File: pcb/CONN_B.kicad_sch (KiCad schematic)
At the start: 8 parts, among them J2 USB_B, J3 6437288-4, J4 Conn_ARM_SWD_TagConnect_TC2030

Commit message: power done
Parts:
- removed R1, R2, R3, R4: 47R, Resistor_SMD:R_0603_1608Metric_Pad0.98x0.95mm_HandSolder, symbol Device:R
- added JP2: SolderJumper_2_Open, symbol Jumper:SolderJumper_2_Open
- J4: value Conn_ARM_SWD_TagConnect_TC2030 -> TagConnect
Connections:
- net 3V3: now also JP2.2 (B); no longer J4.1 (VCC)
- net STM_NRST: now also J3.19, J4.3 (~{RESET})
- net STM_SWDCLK: now also J3.17, J4.4 (SWCLK)
- net STM_SWDIO: now also J3.16, J4.2 (SWDIO)
- net STM_SWO: now also J3.18, J4.6 (SWO)
- net GPIO_3V3: now reaches J3.11
- new net: J4.1 (VCC), JP2.1 (A)
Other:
- moved on the sheet: C1, J2, J3, J4

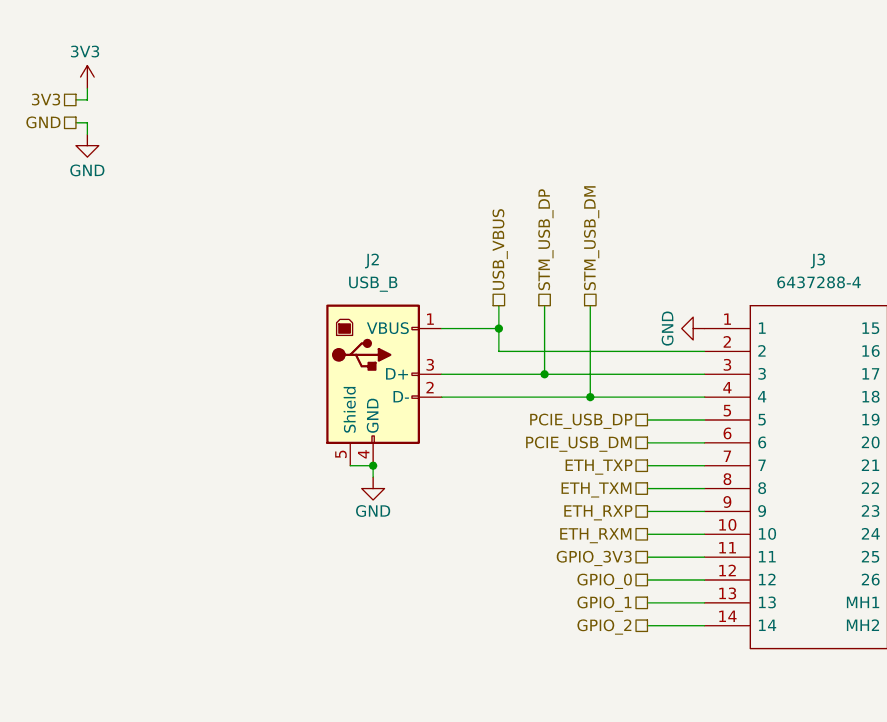
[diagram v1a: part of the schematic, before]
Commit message: added USB protection, reviewed LSD and HSD, improved input TVS footprint
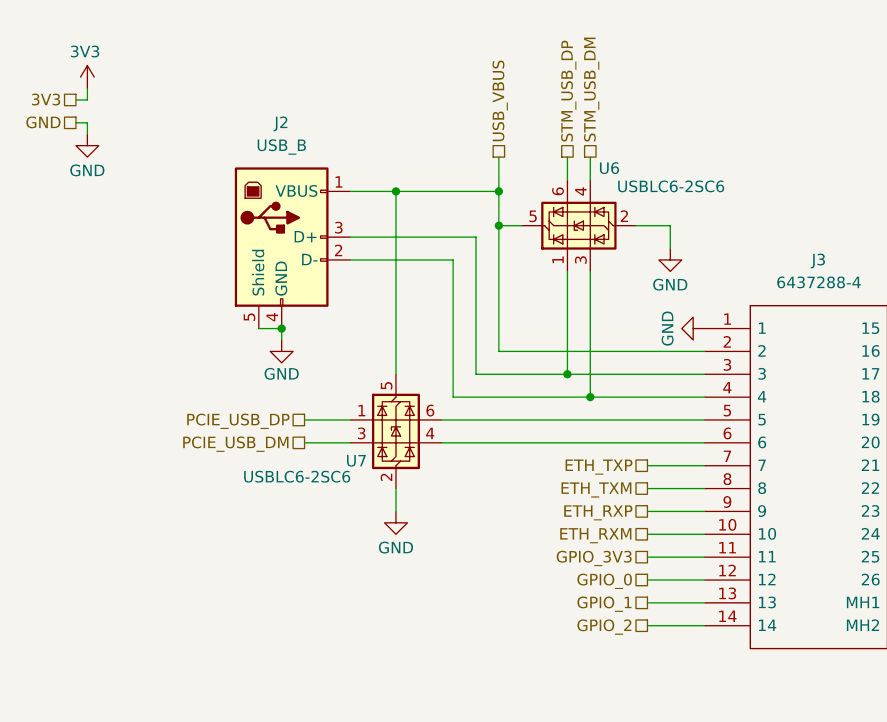
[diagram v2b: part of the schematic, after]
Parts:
- added U6, U7: USBLC6-2SC6, Package_TO_SOT_SMD:SOT-23-6, symbol Power_Protection:USBLC6-2SC6
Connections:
- net GND: now also U6.2 (GND), U7.2 (GND)
- net PCIE_USB_DM: now also U7.3 (I/O2); no longer J3.6
- net PCIE_USB_DP: now also U7.1 (I/O1); no longer J3.5
- net STM_USB_DM: now also U6.4 (I/O2); no longer J2.2 (D-), J3.4
- net STM_USB_DP: now also U6.6 (I/O1); no longer J2.3 (D+), J3.3
- net USB_VBUS: now also U6.5 (VBUS), U7.5 (VBUS)
- new net: J2.2 (D-), J3.4, U6.3 (I/O2)
- new net: J2.3 (D+), J3.3, U6.1 (I/O1)
- new net: J3.5, U7.6 (I/O1)
- new net: J3.6, U7.4 (I/O2)
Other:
- moved on the sheet: J2

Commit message: reannotated, updated some symbols
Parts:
- removed JP2: SolderJumper_2_Open, symbol Jumper:SolderJumper_2_Open
- added JP1, JP2, JP3, JP4, JP5: SolderJumper_2_Bridged, Jumper:SolderJumper-2_P1.3mm_Bridged_RoundedPad1.0x1.5mm, symbol Jumper:SolderJumper_2_Bridged
- renumbered U7 to U1, U6 to U2
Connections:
- net 3V3: now also JP5.2 (B)
- net STM_NRST: now also JP4.2 (B); no longer J3.19
- net STM_SWDCLK: now also JP2.2 (B); no longer J3.17
- net STM_SWDIO: now also JP1.2 (B); no longer J3.16
- net STM_SWO: now also JP3.2 (B); no longer J3.18
- net at J4.1 (VCC): now also JP5.1 (A)
- new net: J3.17, JP2.1 (A)
- new net: J3.16, JP1.1 (A)
- new net: J3.18, JP3.1 (A)
- new net: J3.19, JP4.1 (A)

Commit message: minor changes before layout
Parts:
- removed JP5: SolderJumper_2_Bridged, Jumper:SolderJumper-2_P1.3mm_Bridged_RoundedPad1.0x1.5mm, symbol Jumper:SolderJumper_2_Bridged
- added JP5: SolderJumper_2_Open, Jumper:SolderJumper-2_P1.3mm_Open_RoundedPad1.0x1.5mm, symbol Jumper:SolderJumper_2_Open
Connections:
- net 3V3: now also JP5.2 (B)
- net at J4.1 (VCC): now also JP5.1 (A)
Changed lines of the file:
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@@
-	)
-	(symbol
-		(lib_id "Jumper:SolderJumper_2_Bridged")
-		(at 168.91 40.64 0)
-		(unit 1)
-		(exclude_from_sim no)
-		(in_bom no)
-		(on_board yes)
-		(dnp no)
-		(property "Reference" "JP5"
-			(at 165.862 39.37 0)
-			(effects
-				(font
-					(size 1.27 1.27)
-				)
-			)
-		)
-		(property "Value" "SolderJumper_2_Bridged"
-			(at 168.91 36.83 0)
-			(effects
-				(font
-					(size 1.27 1.27)
-				)
-				(hide yes)
-			)
-		)
-		(property "Footprint" "Jumper:SolderJumper-2_P1.3mm_Bridged_RoundedPad1.0x1.5mm"
-			(at 168.91 40.64 0)
-			(effects
-				(font
-					(size 1.27 1.27)
-				)
-				(hide yes)
-			)
-		)
-		(property "Datasheet" "~"
-			(at 168.91 40.64 0)
-			(effects
-				(font
-					(size 1.27 1.27)
-				)
-				(hide yes)
-			)
-		)
-		(property "Description" "Solder Jumper, 2-pole, closed/bridged"
-			(at 168.91 40.64 0)
-			(effects
-				(font
-					(size 1.27 1.27)
-				)
-				(hide yes)
-			)
-		)
-		(pin "1"
-		)
-		(pin "2"
-		)
-		(instances
-			(project "NCU"
-				(path "/3aee14c3-5480-4f7c-989e-3fef81779034/58530478-b11f-47ae-90e9-56fd185c9f38"
-					(reference "JP5")
-					(unit 1)
-				)
-			)
-		)
 	)
 	(symbol
@@
 					(unit 1)
 				)
+			)
+		)
+	)
+	(symbol
+		(lib_id "Jumper:SolderJumper_2_Open")
+		(at 168.91 40.64 0)
+		(unit 1)
+		(exclude_from_sim no)
+		(in_bom no)
+		(on_board yes)
+		(dnp no)
+		(fields_autoplaced yes)
+		(property "Reference" "JP5"
+			(at 168.91 34.29 0)
+			(effects
+				(font
+					(size 1.27 1.27)
+				)
+			)
+		)
+		(property "Value" "SolderJumper_2_Open"
+			(at 168.91 36.83 0)
+			(effects
+				(font
+					(size 1.27 1.27)
+				)
+			)
+		)
+		(property "Footprint" "Jumper:SolderJumper-2_P1.3mm_Open_RoundedPad1.0x1.5mm"
+			(at 168.91 40.64 0)
+			(effects
+				(font
+					(size 1.27 1.27)
+				)
+				(hide yes)
+			)
+		)
+		(property "Datasheet" "~"
+			(at 168.91 40.64 0)
+			(effects
+				(font
+					(size 1.27 1.27)
+				)
+				(hide yes)
+			)
+		)
+		(property "Description" "Solder Jumper, 2-pole, open"
+			(at 168.91 40.64 0)
+			(effects
+				(font
+					(size 1.27 1.27)
+				)
+				(hide yes)
+			)
+		)
+		(pin "1"
+		)
+		(pin "2"
+		)
+		(instances
+			(project ""
+				(path "/3aee14c3-5480-4f7c-989e-3fef81779034/58530478-b11f-47ae-90e9-56fd185c9f38"
+					(reference "JP5")
+					(unit 1)
+				)

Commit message: sd card slot initial attempt (I meant SIM before)
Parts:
- J2: footprint Connector_USB:USB_B_Lumberg_2411_02_Horizontal -> Connector_USB:USB_B_OST_USB-B1HSxx_Horizontal
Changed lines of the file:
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@@
 			)
 		)
-		(property "Footprint" "Connector_USB:USB_B_Lumberg_2411_02_Horizontal"
+		(property "Footprint" "Connector_USB:USB_B_OST_USB-B1HSxx_Horizontal"
 			(at 45.72 38.1 0)
 			(effects

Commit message: rerouted usb and comms signals
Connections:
- net PCIE_USB_DM: now also U1.4 (I/O2); no longer U1.3 (I/O2)
- net PCIE_USB_DP: now also U1.6 (I/O1); no longer U1.1 (I/O1)
- net at J3.5: now also U1.1 (I/O1); no longer U1.6 (I/O1)
- net at J3.6: now also U1.3 (I/O2); no longer U1.4 (I/O2)

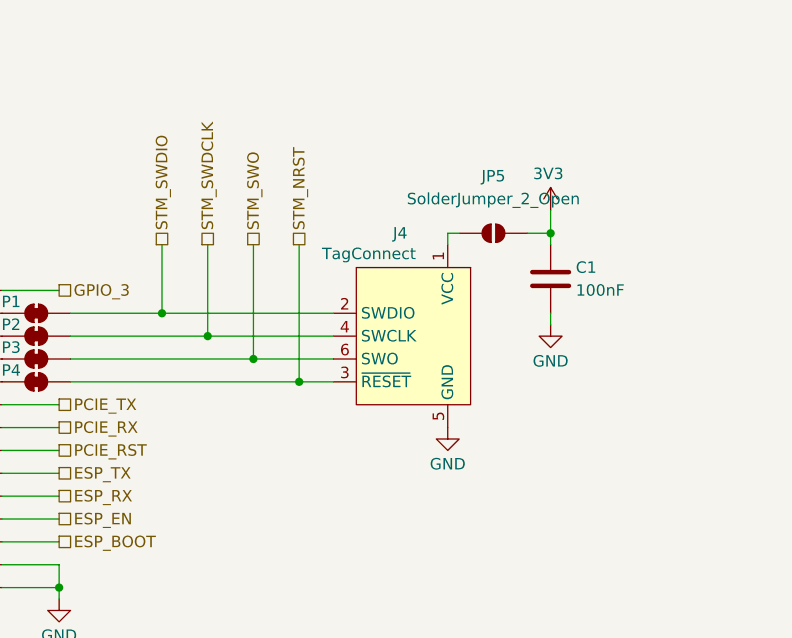
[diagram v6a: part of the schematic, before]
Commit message: changed swd connector, removed ground trace between eth and usb lines
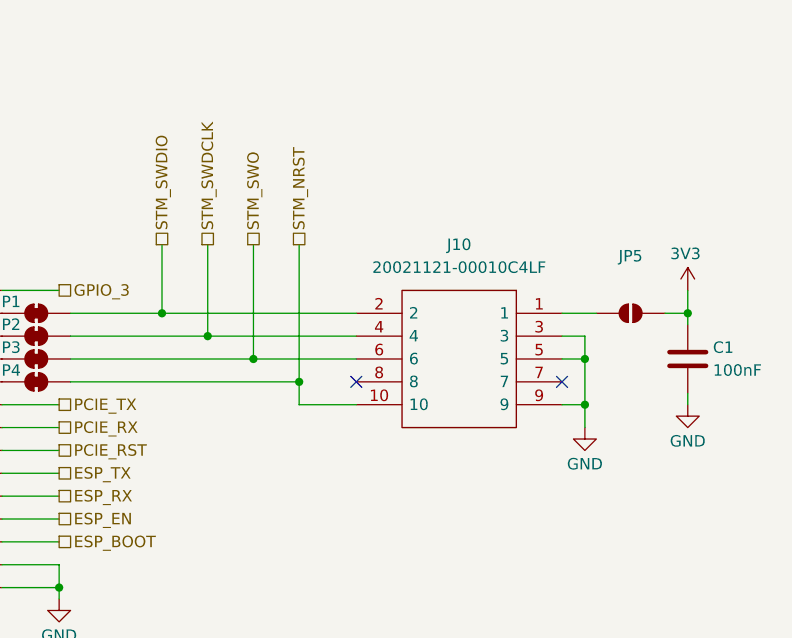
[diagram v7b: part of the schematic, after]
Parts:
- removed J4: TagConnect, Connector:Tag-Connect_TC2030-IDC-FP_2x03_P1.27mm_Vertical, symbol Connector:Conn_ARM_SWD_TagConnect_TC2030
- added J10: 20021121-00010C4LF, 2002112100010C4LF, symbol 0_SamacSys_Parts:20021121-00010C4LF
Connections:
- net GND: now also J10.3, J10.5, J10.9
- net STM_NRST: now also J10.10
- net STM_SWDCLK: now also J10.4
- net STM_SWDIO: now also J10.2
- net STM_SWO: now also J10.6
- net at JP5.1 (A): now also J10.1
- no-connect marks 0 -> 2
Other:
- moved on the sheet: C1, JP5

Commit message: updates from bom release
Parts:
- C1: value 100nF -> 100n
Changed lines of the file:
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@@
 			)
 		)
-		(property "Value" "100nF"
+		(property "Value" "100n"
 			(at 193.294 55.88 0)
 			(effects
